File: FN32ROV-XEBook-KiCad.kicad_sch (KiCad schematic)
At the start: 60 parts, among them J2 USB-C 16P, Q1 UMH3NTN, Q2 DMP2035U-7, Q3 DMG2302U, U1 ESP32-WROVER-E, U2 CP2102N-A02-GQFN24R, U3 74LS07DR, U4 74LS07DR, U5 XC6220B331MR

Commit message: Move resistor/cap reference & value beside the body, fix long-label overlaps
Based on the user's manual fix to R10 in the KiCad GUI: for vertical R/C
parts, keep the symbol itself at rotation 0 (unchanged) but move
Reference/Value to the left/right of the body (rotated 90°, ~2.54mm
offset) instead of above/below. This keeps them out of the path of the
net-name labels extending vertically from the pins, which is what was
causing "smashed together" text throughout the sheet.

That fix alone wasn't sufficient though: net labels that read "backward"
from their stub anchor (see label_orientation's "right"-justify case)
sweep toward the component body/opposite pin, and 5.08mm of stub isn't
enough clearance for anything longer than ~4 characters. Long names like
CP2102_VBUS_SENSE or IO36/MCTRL were sweeping straight through the
component and into whatever sits on the other side.

Fixed with a length-tiered stub (grid-aligned multiples of 12.7mm,
scoped to only the "backward"-justified pin so short/forward labels are
unaffected) and applied it uniformly via the shared place_component
path so both the real schematic and the collision-detection helper stay
in sync. Surfaced several genuine spacing bugs in the process (R4/R8,
R7/C3, C10/C12, D4/D5/D6, and the reset circuit sitting too close to a
row I'd shifted) where components were placed exactly at the old stub's
reach limit -- fixed each by adding clearance or swapping which net
gets the long-reaching side.

ERC clean (1 expected violation: IO12/TDI). One minor cosmetic case
remains (very long forward-justified labels like SIO_DATAIN start close
enough to the component body to look a little tight, though nothing
actually overlaps electrically or with the reference/value text) --
left for manual touch-up.

Co-Authored-By: Claude Sonnet 5 <noreply@anthropic.com>
Claude-Session: https://claude.ai/code/session_01ATUvQCobb1cVELUyjLrcQZ
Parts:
- D4, D5, D6: footprint Diode_SMD:D_SOD-523 -> (none)
- D7, D8: footprint Diode_SMD:D_SOD-323 -> (none)
- J2: footprint LocalOverrides:USB_C_Receptacle_HCTL_HC-TYPE-C-16P-01A -> (none)
- Q1: footprint Package_TO_SOT_SMD:SOT-363_SC-70-6 -> (none)
- Q2, Q3: footprint Package_TO_SOT_SMD:SOT-23 -> (none)
- SD1: footprint Connector_Card:microSD_HC_Hirose_DM3D-SF -> (none)
- U1: footprint Espressif:ESP32-WROVER-E -> (none)
- U2: footprint Package_DFN_QFN:QFN-24-1EP_4x4mm_P0.5mm_EP2.6x2.6mm -> (none)
- U3, U4: footprint Package_SO:SOIC-14_3.9x8.7mm_P1.27mm -> (none)
- U5: footprint Package_TO_SOT_SMD:SOT-23-5 -> (none)
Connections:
- net GND: now also C10.1; no longer C10.2
- net PWR_SW_VCC: now also C10.2; no longer C10.1

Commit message: Complete PCB routing and fix component/footprint errors
- Fix C12: correct value/footprint to 47uF 10V Tantalum 7343 (was
  mistakenly authored as 4.7uF 10V ceramic 0402)
- Fix Q2/Q3 pin numbering: Device:Q_PMOS/Q_NMOS symbols use G/D/S pin
  numbers but their SOT-23 footprints use 1/2/3, so no net was ever
  assigned to either part's pads. Remapped per the original DipTrace
  netlist's pin-to-function mapping (1=G, 2=S, 3=D).
- Assign missing Footprint properties for D4-D8, J2, Q1-Q3, SD1, U1-U5
  so PCB stays in sync with the schematic via Update PCB from Schematic
- Complete PCB routing - all nets connected, 0 DRC errors
- Add scoped design rule easing J2's NPTH-to-GND-pad hole clearance to
  0.15mm (inherent to the real connector's geometry; verified within
  JLCPCB's standard capability), without loosening the board's global rule
- Verify full netlist against the original FN32ROV-1.7.1 DipTrace export:
  no missing or incorrect connections, only expected renames/pin-numbering
  differences between library parts

Co-Authored-By: Claude Sonnet 5 <noreply@anthropic.com>
Claude-Session: https://claude.ai/code/session_01ATUvQCobb1cVELUyjLrcQZ
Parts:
- C12: value 4.7uF 10V -> 47uF 10V; footprint Capacitor_SMD:C_0402_1005Metric -> Capacitor_Tantalum_SMD:CP_EIA-7343-31_Kemet-D
- D4, D5, D6: footprint (none) -> Diode_SMD:D_SOD-523
- D7, D8: footprint (none) -> Diode_SMD:D_SOD-323
- J2: footprint (none) -> LocalOverrides:USB_C_Receptacle_HCTL_HC-TYPE-C-16P-01A
- Q1: footprint (none) -> Package_TO_SOT_SMD:SOT-363_SC-70-6
- Q2, Q3: footprint (none) -> Package_TO_SOT_SMD:SOT-23
- SD1: footprint (none) -> Connector_Card:microSD_HC_Hirose_DM3D-SF
- U1: footprint (none) -> Espressif:ESP32-WROVER-E
- U2: footprint (none) -> Package_DFN_QFN:QFN-24-1EP_4x4mm_P0.5mm_EP2.6x2.6mm
- U3, U4: footprint (none) -> Package_SO:SOIC-14_3.9x8.7mm_P1.27mm
- U5: footprint (none) -> Package_TO_SOT_SMD:SOT-23-5
- renumbered J_BTN to J_BTN1, J_LED to J_LED1, J_PWR to J_PWR1, J_SD to J_SD1, J_SIO to J_SIO1
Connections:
- net GND: now also Q3.2 (S); no longer Q3.S
- net PWR_SW_VCC: now also Q2.2 (S); no longer Q2.S
- net Q2_GATE: now also Q2.1 (G), Q3.3 (D); no longer Q2.G, Q3.D
- net Q3_GATE: now also Q3.1 (G); no longer Q3.G
- net VCC_BUF: now also Q2.3 (D); no longer Q2.D
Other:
- moved on the sheet: C1, C10, C11, C12, C3, C4, C5, C6, C7, C8, C9, D4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

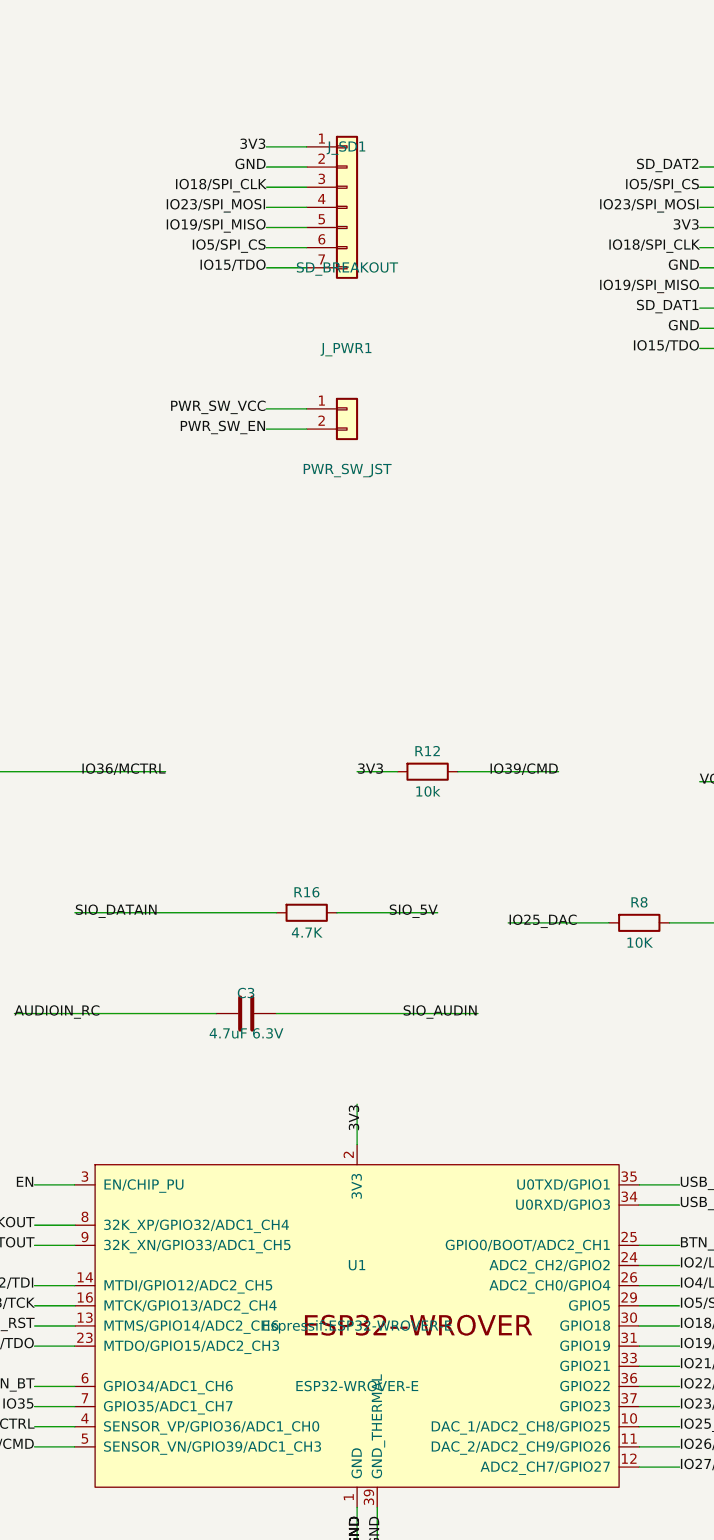
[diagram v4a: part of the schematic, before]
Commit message: Swap external SD header to JST PH, add missing R11/R17, resize mounting holes to M2, add antenna notch, switch to WROVER-IE, center back logo
- J_SD1: replace 2.54mm pin header with JST PH 7-pin (matches BTN/LED/PWR_SW JST connectors)
- Add R11 (CP2102 VBUS-sense) and R17 (SPI MISO pull-up), previously missing from PCB despite valid schematic footprints
- MH1-MH4: resize from 2.5mm bare holes to MountingHole_2.2mm_M2
- Add J2 USB-C NPTH clearance rule and SD1 board-edge clearance rule to .kicad_dru
- Cut board-edge notch under U1's antenna keepout zone to remove FR4 substrate from under the ESP32 antenna
- U1: ESP32-WROVER-E to ESP32-WROVER-IE-N16R8 (adds U.FL external antenna option alongside onboard antenna)
- Add front/back copper pours
- Import and center Sideburn Studios back-silkscreen logo (Graphics/FujinetXEBOOKLogo)
- Full DRC/ERC/schematic-parity verification against schematic and against original FujiNet FN32ROV-1.7.1 netlist: 0 unconnected items, 0 electrical violations

Co-Authored-By: Claude Sonnet 5 <noreply@anthropic.com>
Claude-Session: https://claude.ai/code/session_01GM9FQ1pLMMKCV3Qfiq1ore
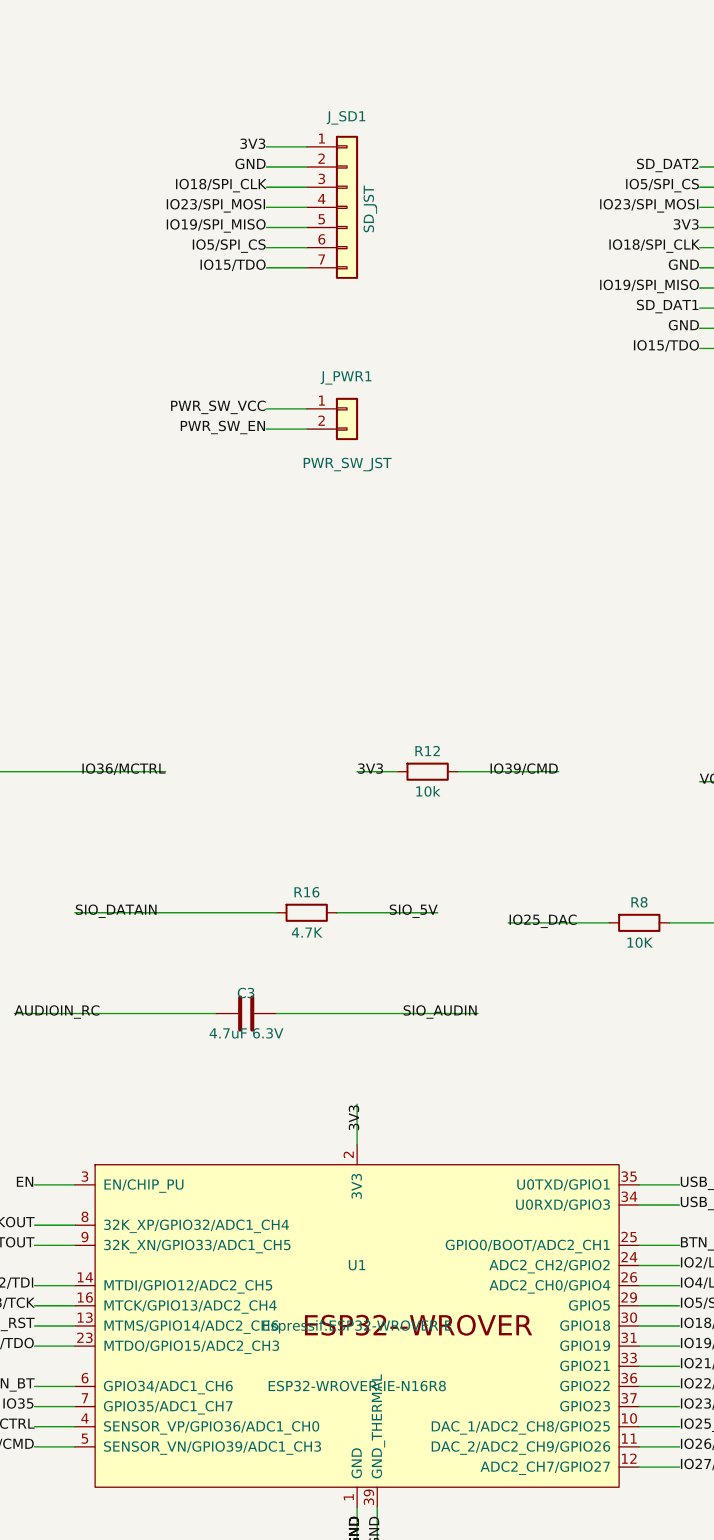
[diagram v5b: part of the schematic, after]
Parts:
- J_SD1: value SD_BREAKOUT -> SD_JST; footprint Connector_PinHeader_2.54mm:PinHeader_1x07_P2.54mm_Vertical -> Connector_JST:JST_PH_S7B-PH-K_1x07_P2.00mm_Horizontal
- U1: value ESP32-WROVER-E -> ESP32-WROVER-IE-N16R8
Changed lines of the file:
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@@
 			)
 		)
-		(pin "G"
+		(pin "1"
 		)
-		(pin "D"
+		(pin "3"
 		)
-		(pin "S"
+		(pin "2"
 		)
 		(instances
@@
 			)
 		)
-		(property "Value" "ESP32-WROVER-E"
+		(property "Value" "ESP32-WROVER-IE-N16R8"
 			(at 153.67 199.39 0)
 			(effects
@@
 		(dnp no)
 		(property "Reference" "J_PWR1"
-			(at 152.4 68.58 0)
+			(at 152.4 72.136 0)
 			(effects
 				(font
@@
 		)
 		(property "Value" "PWR_SW_JST"
-			(at 152.4 83.82 0)
+			(at 152.4 83.058 0)
 			(effects
 				(font
@@
 			)
 		)
-		(pin "G"
+		(pin "1"
 		)
-		(pin "D"
+		(pin "3"
 		)
-		(pin "S"
+		(pin "2"
 		)
 		(instances
@@
 		(dnp no)
 		(property "Reference" "J_SD1"
-			(at 152.4 43.18 0)
+			(at 152.4 39.37 0)
 			(effects
 				(font
@@
 			)
 		)
-		(property "Value" "SD_BREAKOUT"
-			(at 152.4 58.42 0)
+		(property "Value" "SD_JST"
+			(at 155.194 51.054 90)
 			(effects
 				(font
@@
 			)
 		)
-		(property "Footprint" "Connector_PinHeader_2.54mm:PinHeader_1x07_P2.54mm_Vertical"
+		(property "Footprint" "Connector_JST:JST_PH_S7B-PH-K_1x07_P2.00mm_Horizontal"
 			(at 152.4 50.8 0)
 			(effects
